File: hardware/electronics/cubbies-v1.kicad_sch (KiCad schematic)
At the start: 17 parts, among them J1 I2C expansion Qwiic/STEMMA QT, Q1 AO3400A, SW1 TTP223 touch module, U1 XIAO ESP32-C3, U2 GY-521 MPU6050 IMU module, U3 GY-302 BH1750 light module (t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

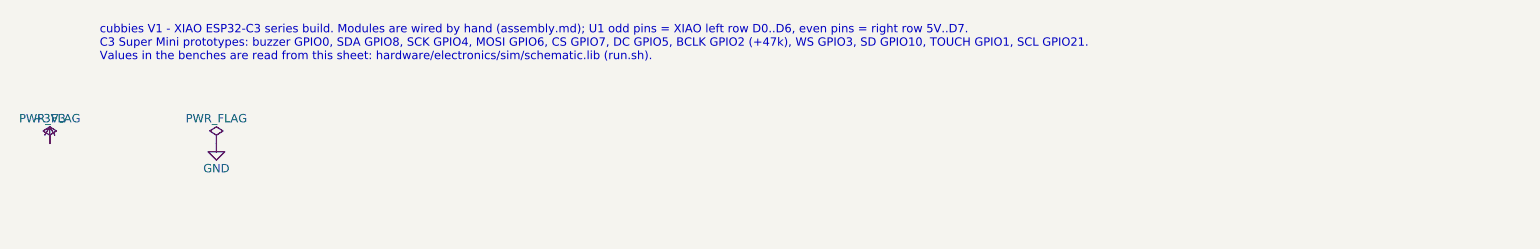
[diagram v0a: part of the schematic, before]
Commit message: fix(hardware): address local review on the schematic brick
Stale calculations README, exact I2C conductances, parser hardening and self-test,
visible kicad-cli fallback, bench headers name the schematic refs, pin-order note.

Co-Authored-By: Claude Opus 5.5 <noreply@anthropic.com>
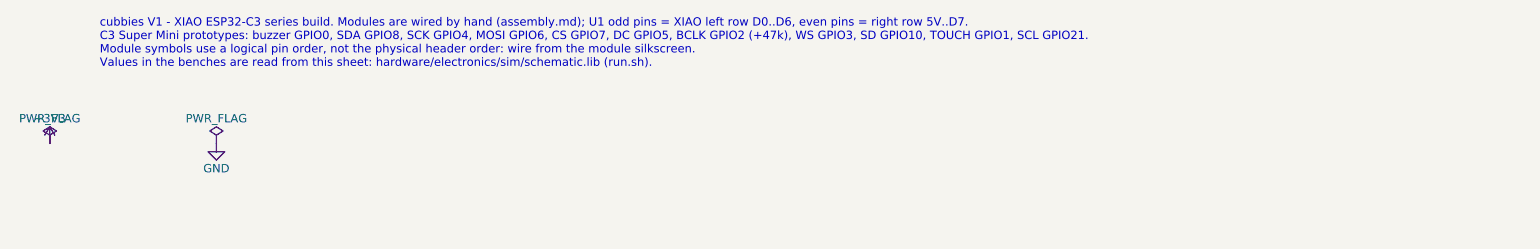
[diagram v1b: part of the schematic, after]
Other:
- note added: "cubbies V1 - XIAO ESP32-C3 series build. Modules are wired by hand (assembly.md); U1 odd pins = XIAO left row D0..D6, even pins = right row 5V..D7. C3 Super Mini prototypes: buzzer GPIO0, SDA GPIO8, SCK GPIO4, MOSI GPIO6, CS GPIO7, DC GPIO5, BCLK GPIO2 (+47k), WS GPIO3, SD GPIO10, TOUCH GPIO1, SCL GPIO21. Module symbols use a logical pin order, not the physical header order: wire from the module 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"
- note removed: "cubbies V1 - XIAO ESP32-C3 series build. Modules are wired by hand (assembly.md); U1 odd pins = XIAO left row D0..D6, even pins = right row 5V..D7. C3 Super Mini prototypes: buzzer GPIO0, SDA GPIO8, SCK GPIO4, MOSI GPIO6, CS GPIO7, DC GPIO5, BCLK GPIO2 (+47k), WS GPIO3, SD GPIO10, TOUCH GPIO1, SCL GPIO21. Values in the benches are read from this sheet: hardware/electronics/sim/schematic.lib (run.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"

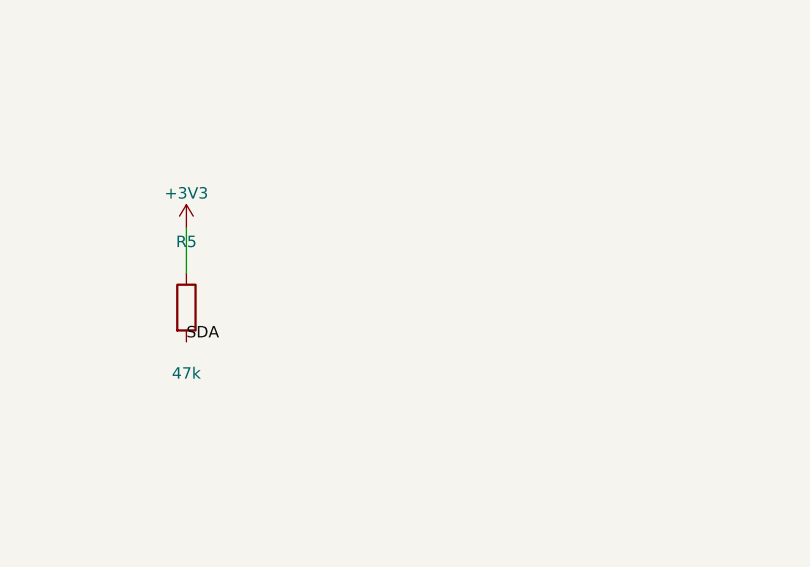
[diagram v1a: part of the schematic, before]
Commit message: docs(hardware): close CDR paper items — XC6210 LDO, GPIO8 pull-up R6, second method (#30, #31, #32) (#38)
* docs(hardware): close CDR paper items — XC6210 LDO, GPIO8 pull-up R6, closed-form second method (#30, #31, #32)

The XIAO ESP32-C3 LDO is a Torex XC6210B332MR, not a TLV75733 (C-0013,
supersedes C-0002); J1 budget kept provisional until the bench Tj
measurement. GPIO8 has no pull-up on the XIAO: R6 10k added (C-0014).
crosscheck.py recomputes every Tier 1 corner without SPICE (C-0015).

Co-Authored-By: Claude Opus 5.5 <noreply@anthropic.com>

* fix(hardware): carry the XC6210 rail window to every bench, harden the second method

Review-local findings: buzzer/C-0005/C-0010 corners at 3.234-3.366 V,
honest floating-input control, VIH 2.525 V, crosscheck row counts,
tighter tolerances, low-time sign check, test_crosscheck.py; stale
second-engine and corner-count docs.

Co-Authored-By: Claude Opus 5.5 <noreply@anthropic.com>

* fix(hardware): parse bench cells without a backtracking regex (SonarQube hotspot)

Co-Authored-By: Claude Opus 5.5 <noreply@anthropic.com>

* docs(review): local review report for the CDR paper items

Co-Authored-By: Claude Opus 5.5 <noreply@anthropic.com>

---------

Co-authored-by: Claude Opus 5.5 <noreply@anthropic.com>
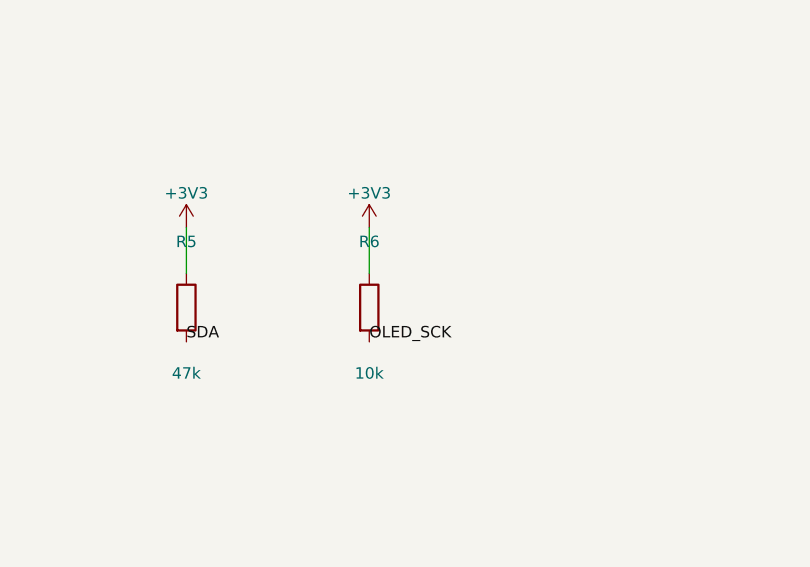
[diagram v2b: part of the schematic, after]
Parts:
- added R6: 10k, Resistor_THT:R_Axial_DIN0207_L6.3mm_D2.5mm_P7.62mm_Horizontal, symbol Device:R
- U1: Justification Odd pins = left row D0..D6 (GPIO2,3,4,5,6,7,21); even pins = right row 5V,GND,3V3,D10,D9,D8,D7 (5V,GND,3V3,GPIO10,9,8,20). 3V3 from the onboard TLV75733 (C-0001, C-0002). ADR-0003 board; pin map electronics-spec.md GPIO contract (ADR-0007, ADR-0015) -> Odd pins = left row D0..D6 (GPIO2,3,4,5,6,7,21); even pins = right row 5V,GND,3V3,D10,D9,D8,D7 (5V,GND,3V3,GPIO10,9,8,20). 3V3 from the onboard Torex XC6210B332MR behind a Schottky and a 500 mA PTC (Seeed schematic; C-0001, C-0013). ADR-0003 board; pin map electronics-spec.md GPIO contract (ADR-0007, ADR-0015)
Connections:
- net +3V3: now also R6.1
- net OLED_SCK: now also R6.2
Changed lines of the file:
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@@
 (kicad_sch (version 20250114) (generator "eeschema") (generator_version "9.0") (paper "A3")
 (title_block (title "cubbies V1") (date "2026-10-16") (rev "1") (comment 1 "GPIO contract: docs/hardware/electronics-spec.md (ADR-0015)") (comment 2 "Calculations: docs/hardware/calculations/log.md"))
-(symbol (lib_id "Connector_Generic:Conn_02x07_Odd_Even") (at 132.07999999999998 116.83999999999999 0) (unit 1) (exclude_from_sim yes) (in_bom yes) (on_board yes) (dnp no) (property "Reference" "U1" (at 132.07999999999998 105.71999999999998 0) (effects (font (size 1.27 1.27))))(property "Value" "XIAO ESP32-C3" (at 132.07999999999998 127.96 0) (effects (font (size 1.27 1.27))))(property "Footprint" "" (at 132.07999999999998 116.83999999999999 0) (effects (font (size 1.27 1.27)) (hide yes)))(property "Justification" "Odd pins = left row D0..D6 (GPIO2,3,4,5,6,7,21); even pins = right row 5V,GND,3V3,D10,D9,D8,D7 (5V,GND,3V3,GPIO10,9,8,20). 3V3 from the onboard TLV75733 (C-0001, C-0002). ADR-0003 board; pin map electronics-spec.md GPIO contract (ADR-0007, ADR-0015)" (at 132.07999999999998 116.83999999999999 0) (effects (font (size 1.27 1.27)) (hide yes))) (pin "1")(pin "3")(pin "5")(pin "7")(pin "9")(pin "11")(pin "13")(pin "2")(pin "4")(pin "6")(pin "8")(pin "10")(pin "12")(pin "14") (instances (project "cubbies-v1" (path "/9f4f8700-33e0-4526-9ff3-0950706a27c7" (reference "U1") (unit 1)))))
+(symbol (lib_id "Connector_Generic:Conn_02x07_Odd_Even") (at 132.07999999999998 116.83999999999999 0) (unit 1) (exclude_from_sim yes) (in_bom yes) (on_board yes) (dnp no) (property "Reference" "U1" (at 132.07999999999998 105.71999999999998 0) (effects (font (size 1.27 1.27))))(property "Value" "XIAO ESP32-C3" (at 132.07999999999998 127.96 0) (effects (font (size 1.27 1.27))))(property "Footprint" "" (at 132.07999999999998 116.83999999999999 0) (effects (font (size 1.27 1.27)) (hide yes)))(property "Justification" "Odd pins = left row D0..D6 (GPIO2,3,4,5,6,7,21); even pins = right row 5V,GND,3V3,D10,D9,D8,D7 (5V,GND,3V3,GPIO10,9,8,20). 3V3 from the onboard Torex XC6210B332MR behind a Schottky and a 500 mA PTC (Seeed schematic; C-0001, C-0013). ADR-0003 board; pin map electronics-spec.md GPIO contract (ADR-0007, ADR-0015)" (at 132.07999999999998 116.83999999999999 0) (effects (font (size 1.27 1.27)) (hide yes))) (pin "1")(pin "3")(pin "5")(pin "7")(pin "9")(pin "11")(pin "13")(pin "2")(pin "4")(pin "6")(pin "8")(pin "10")(pin "12")(pin "14") (instances (project "cubbies-v1" (path "/9f4f8700-33e0-4526-9ff3-0950706a27c7" (reference "U1") (unit 1)))))
 (label "SDA" (at 127.0 109.22 180) (effects (font (size 1.27 1.27)) (justify right bottom)))
 (label "OLED_CS" (at 127.0 111.76 180) (effects (font (size 1.27 1.27)) (justify right bottom)))
@@
 (symbol (lib_id "power:+3V3") (at 132.08 196.85 0) (unit 1) (exclude_from_sim no) (in_bom yes) (on_board yes) (dnp no) (property "Reference" "#PWR16" (at 132.08 196.85 0) (effects (font (size 1.27 1.27)) (hide yes))) (property "Value" "+3V3" (at 132.08 193.04 0) (effects (font (size 1.27 1.27)))) (pin "1") (instances (project "cubbies-v1" (path "/9f4f8700-33e0-4526-9ff3-0950706a27c7" (reference "#PWR16") (unit 1)))))
 (label "SDA" (at 132.08 209.55 0) (effects (font (size 1.27 1.27)) (justify left bottom)))
+(symbol (lib_id "Device:R") (at 152.4 205.74 0) (unit 1) (exclude_from_sim no) (in_bom yes) (on_board yes) (dnp no) (property "Reference" "R6" (at 152.4 198.43 0) (effects (font (size 1.27 1.27))))(property "Value" "10k" (at 152.4 213.05 0) (effects (font (size 1.27 1.27))))(property "Footprint" "Resistor_THT:R_Axial_DIN0207_L6.3mm_D2.5mm_P7.62mm_Horizontal" (at 152.4 205.74 0) (effects (font (size 1.27 1.27)) (hide yes)))(property "Justification" "OLED_SCK = GPIO8 strapping pin: the XIAO has no pull-up on GPIO8 and the SSD1331 SCK input does not drive it; holds GPIO8 = 1 for download boot (C-0014, issue #31)" (at 152.4 205.74 0) (effects (font (size 1.27 1.27)) (hide yes))) (pin "1")(pin "2") (instances (project "cubbies-v1" (path "/9f4f8700-33e0-4526-9ff3-0950706a27c7" (reference "R6") (unit 1)))))
+(wire (pts (xy 152.4 201.93) (xy 152.4 196.85)) (stroke (width 0) (type default)))
+(symbol (lib_id "power:+3V3") (at 152.4 196.85 0) (unit 1) (exclude_from_sim no) (in_bom yes) (on_board yes) (dnp no) (property "Reference" "#PWR26" (at 152.4 196.85 0) (effects (font (size 1.27 1.27)) (hide yes))) (property "Value" "+3V3" (at 152.4 193.04 0) (effects (font (size 1.27 1.27)))) (pin "1") (instances (project "cubbies-v1" (path "/9f4f8700-33e0-4526-9ff3-0950706a27c7" (reference "#PWR26") (unit 1)))))
+(label "OLED_SCK" (at 152.4 209.55 0) (effects (font (size 1.27 1.27)) (justify left bottom)))
 (symbol (lib_id "Connector_Generic:Conn_01x08") (at 335.28000000000003 91.44 0) (unit 1) (exclude_from_sim yes) (in_bom yes) (on_board yes) (dnp no) (property "Reference" "U2" (at 335.28000000000003 80.32 0) (effects (font (size 1.27 1.27))))(property "Value" "GY-521 MPU6050 IMU module" (at 335.28000000000003 105.1 0) (effects (font (size 1.27 1.27))))(property "Footprint" "" (at 335.28000000000003 91.44 0) (effects (font (size 1.27 1.27)) (hide yes)))(property "Justification" "BOM; I2C 400 kHz addr 0x68 (AD0 pulled down on module); onboard 4.7k/2.2k pull-ups counted (C-0007)" (at 335.28000000000003 91.44 0) (effects (font (size 1.27 1.27)) (hide yes))) (pin "1")(pin "2")(pin "3")(pin "4")(pin "5")(pin "6")(pin "7")(pin "8") (instances (project "cubbies-v1" (path "/9f4f8700-33e0-4526-9ff3-0950706a27c7" (reference "U2") (unit 1)))))
 (wire (pts (xy 330.2 83.82) (xy 330.2 78.74)) (stroke (width 0) (type default)))
